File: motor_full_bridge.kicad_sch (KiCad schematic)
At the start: 0 parts

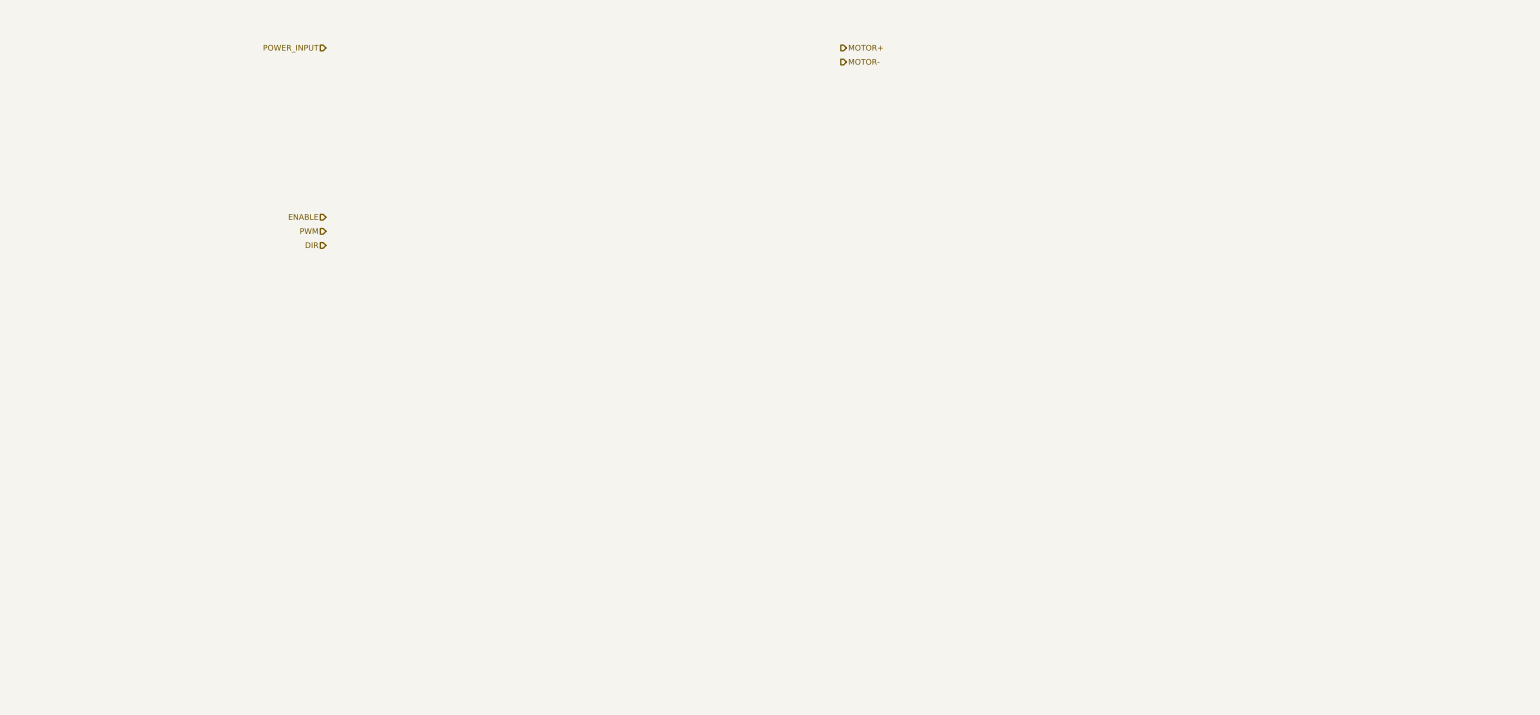
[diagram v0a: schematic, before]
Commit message: Add power stages
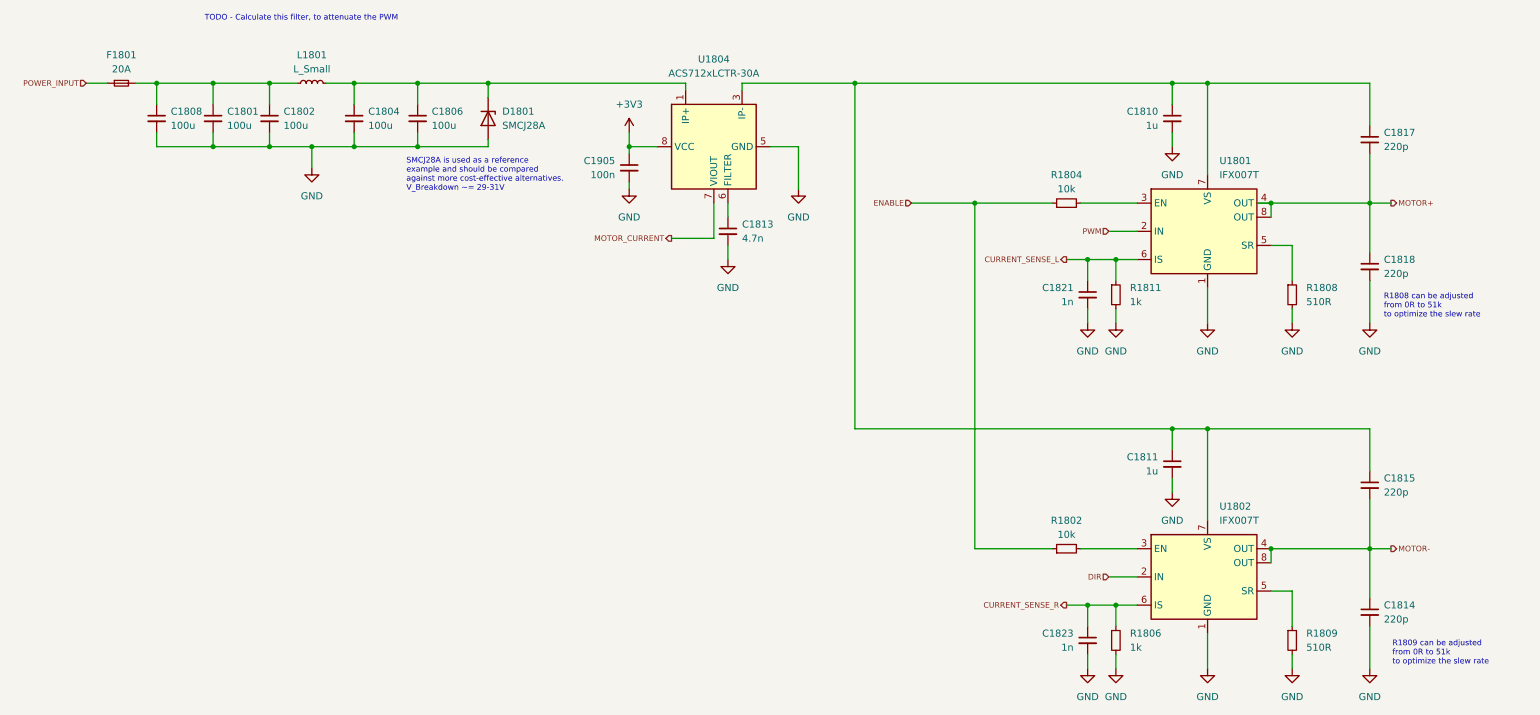
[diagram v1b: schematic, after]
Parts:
- added C1801, C1802, C1804, C1806, C1808: 100u, symbol Device:C_Small
- added C1810, C1811: 1u, symbol Device:C_Small
- added C1813: 4.7n, symbol Device:C_Small
- added C1814, C1815, C1817, C1818: 220p, symbol Device:C_Small
- added C1821, C1823: 1n, symbol Device:C_Small
- added C1905: 100n, symbol Device:C_Small
- added D1801: SMCJ28A, symbol Device:D_Zener
- added F1801: 20A, symbol Device:Fuse_Small
- added L1801: L_Small, symbol Device:L_Small
- added R1802, R1804: 10k, symbol Device:R_Small
- added R1806, R1811: 1k, symbol Device:R_Small
- added R1808, R1809: 510R, symbol Device:R_Small
- added U1801, U1802: IFX007T, symbol Bond_Kicad_Lib:BD_IFX007T
- added U1804: ACS712xLCTR-30A, Package_SO:SOIC-8_3.9x4.9mm_P1.27mm, symbol Sensor_Current:ACS712xLCTR-30A
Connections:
- net DIR: now also U1802.2 (IN)
- net ENABLE: now also R1802.1, R1804.1
- net MOTOR+: now also C1817.2, C1818.1, U1801.4 (OUT), U1801.8 (OUT)
- net MOTOR-: now also C1814.1, C1815.2, U1802.4 (OUT), U1802.8 (OUT)
- net POWER_INPUT: now also F1801.1
- net PWM: now also U1801.2 (IN)
- new net: C1810.1, C1811.1, C1815.1, C1817.1, U1801.7 (VS), U1802.7 (VS), U1804.3 (IP-), U1804.4 (IP-)
- new net: R1809.1, U1802.5 (SR)
- new net: C1801.1, C1802.1, C1808.1, F1801.2, L1801.1
- new net: C1804.1, C1806.1, D1801.1 (K), L1801.2, U1804.1 (IP+), U1804.2 (IP+)
- new net: C1813.1, U1804.6 (FILTER)
- new net: R1804.2, U1801.3 (EN)
- new net: R1808.1, U1801.5 (SR)
- new net: R1802.2, U1802.3 (EN)
- new net +3V3: C1905.1, U1804.8 (VCC)
- new net CURRENT_SENSE_L: C1821.1, R1811.1, U1801.6 (IS)
- new net CURRENT_SENSE_R: C1823.1, R1806.1, U1802.6 (IS)
- new net GND: C1801.2, C1802.2, C1804.2, C1806.2, C1808.2, C1810.2, C1811.2, C1813.2, C1814.2, C1818.2, C1821.2, C1823.2, C1905.2, D1801.2 (A), R1806.2, R1808.2, R1809.2, R1811.2, U1801.1 (GND), U1802.1 (GND), U1804.5 (GND)
- new net MOTOR_CURRENT: U1804.7 (VIOUT)
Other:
- note added: "R1808 can be adjusted from 0R to 51k to optimize the slew rate"
- note added: "R1809 can be adjusted from 0R to 51k to optimize the slew rate"
- note added: "SMCJ28A is used as a reference example and should be compared against more cost-effective alternatives. V_Breakdown ~= 29-31V"
- note added: "TODO - Calculate this filter, to attenuate the PWM"

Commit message: Add power supplies
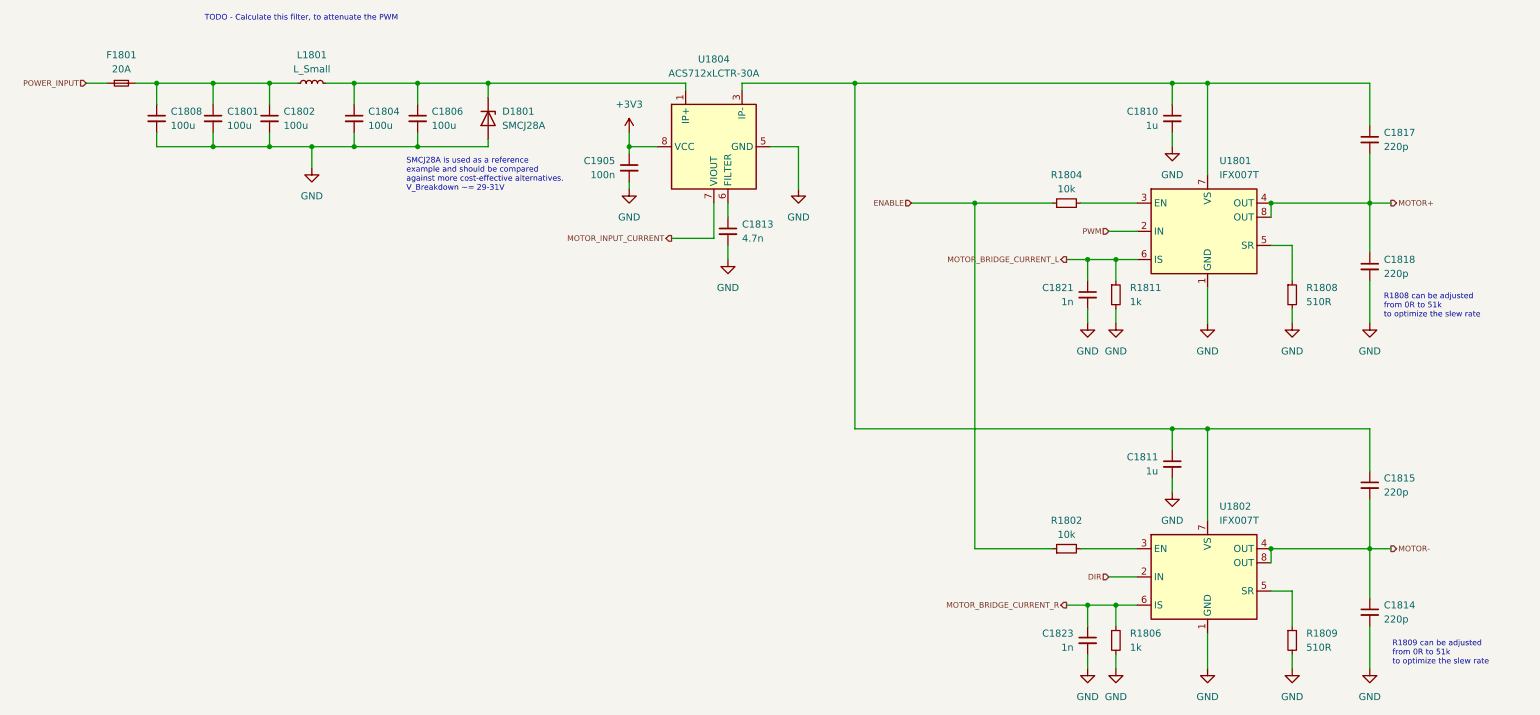
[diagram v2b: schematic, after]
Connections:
- net CURRENT_SENSE_L renamed MOTOR_BRIDGE_CURRENT_L
- net CURRENT_SENSE_R renamed MOTOR_BRIDGE_CURRENT_R
- net MOTOR_CURRENT renamed MOTOR_INPUT_CURRENT
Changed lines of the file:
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@@
 		)
 		(stroke
-			(width 0)
+			(width 0.635)
 			(type default)
 		)
@@
 		)
 		(stroke
-			(width 0)
+			(width 0.635)
 			(type default)
 		)
@@
 		(stroke
 			(width 0.508)
-			(type default)
-		)
-	)
-	(wire
-		(pts
-			(xy 238.76 74.93) (xy 241.3 74.93)
-		)
-		(stroke
-			(width 0)
 			(type default)
 		)
@@
 		)
 	)
-	(hierarchical_label "MOTOR_CURRENT"
+	(hierarchical_label "MOTOR_INPUT_CURRENT"
 		(shape output)
 		(at 133.35 81.28 180)
@@
 		)
 	)
-	(hierarchical_label "CURRENT_SENSE_L"
+	(hierarchical_label "MOTOR_BRIDGE_CURRENT_L"
 		(shape output)
 		(at 204.47 85.09 180)
@@
 		)
 	)
-	(hierarchical_label "CURRENT_SENSE_R"
+	(hierarchical_label "MOTOR_BRIDGE_CURRENT_R"
 		(shape output)
 		(at 204.47 147.32 180)
